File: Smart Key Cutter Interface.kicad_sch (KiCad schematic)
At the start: 9 parts, among them U1 TXU0104PWR, U2 TXU0104PWR, U3 SN74HC4066PWR

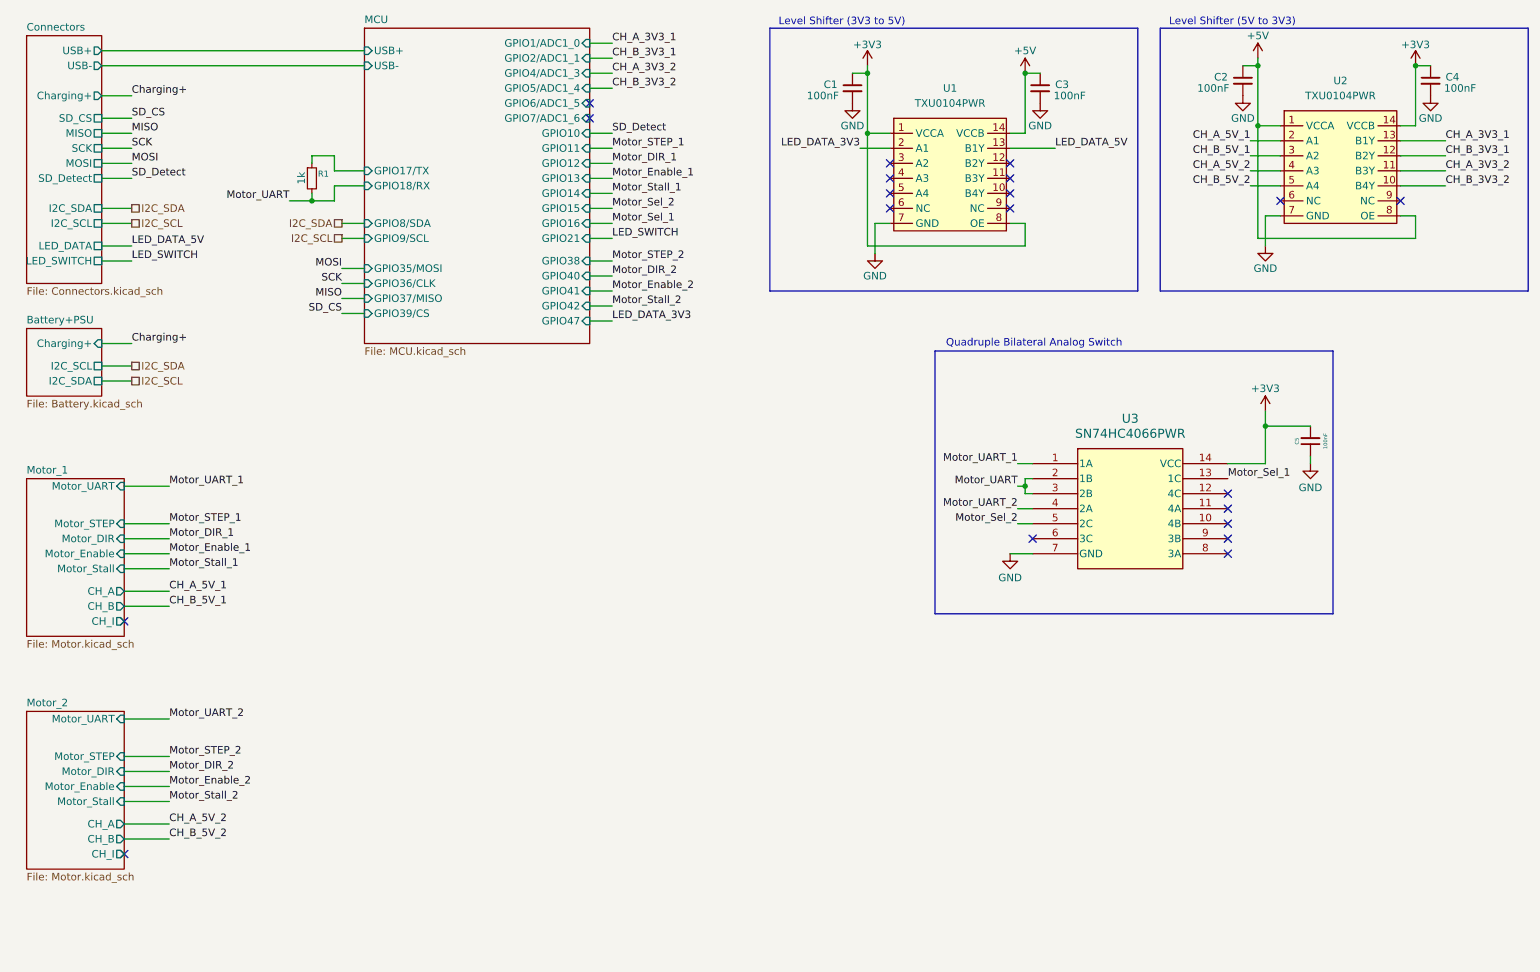
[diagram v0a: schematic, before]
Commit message: Schematic updated for V2.0, updating PCB now
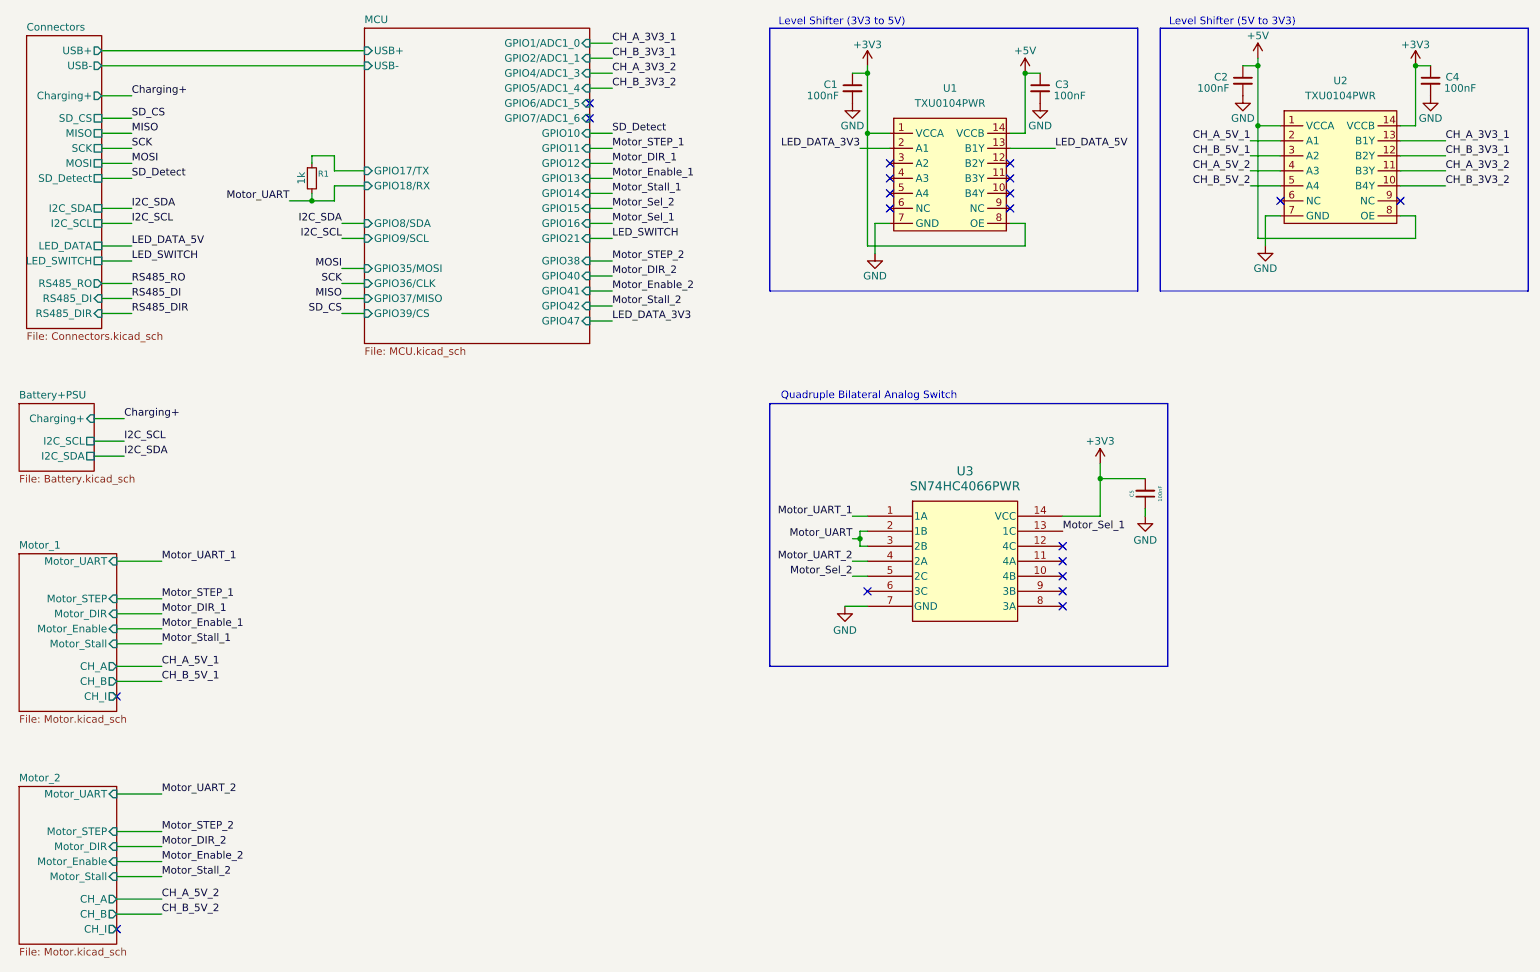
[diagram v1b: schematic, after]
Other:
- sheet Connectors ports: added RS485_DI, RS485_DIR, RS485_RO; removed none
- moved on the sheet: C5, U3
